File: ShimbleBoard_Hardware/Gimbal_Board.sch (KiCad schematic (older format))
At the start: 54 parts, among them Q1 2N3904, Q2 2N3904, Q3 2N3904, Q4 2N3904, Q5 2N3904, Q6 2N3904, Q7 2N3904, Q8 2N3904, U1 TM4C129E_Launchpad, U2 OKI, U3 OKI

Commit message: Noice
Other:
- note added: "Shimble Board"
- moved on the sheet: C1, C2, C3, C4, C5, C6, Conn9A, Conn9B, Conn9C

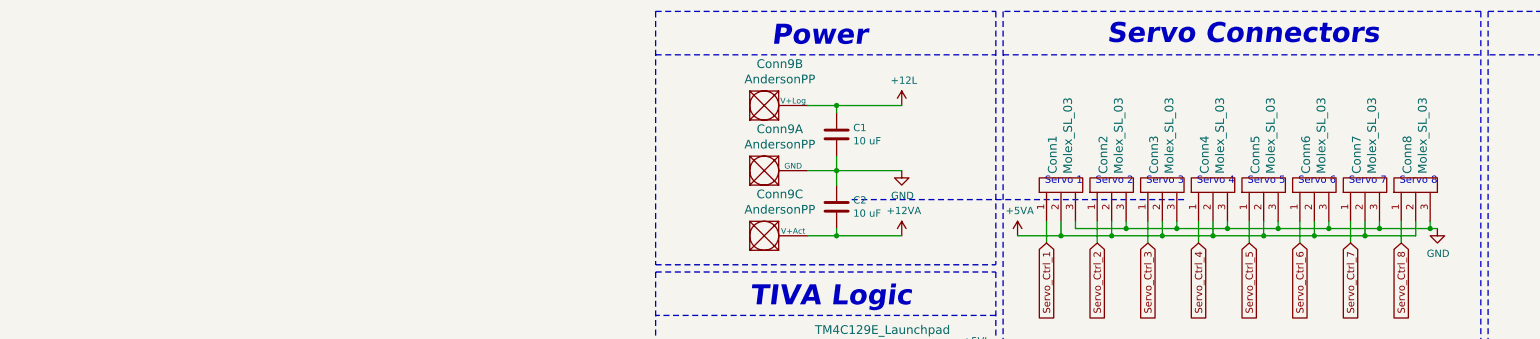
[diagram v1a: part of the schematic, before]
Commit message: Silkscreens Added
Signitures and logo was added.
Schematic cleaned up a little.
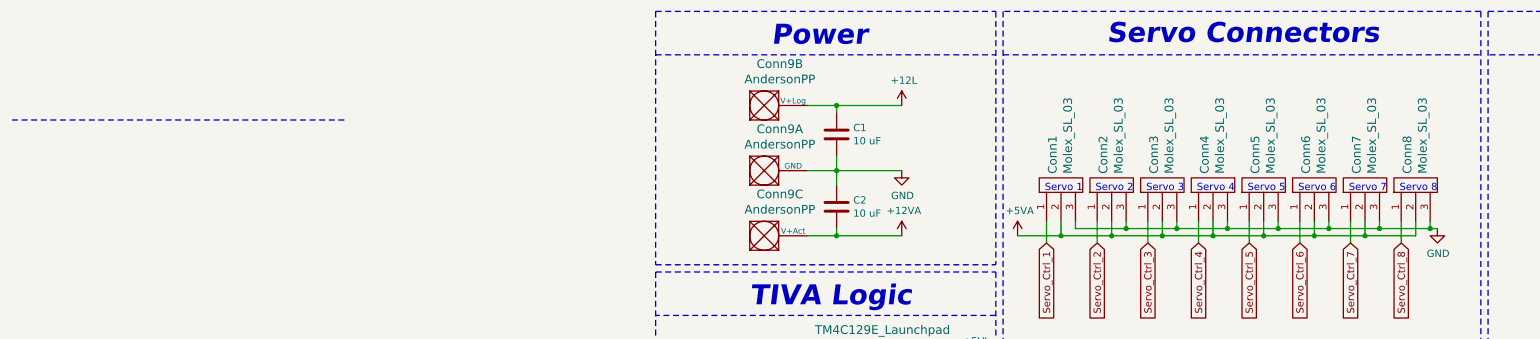
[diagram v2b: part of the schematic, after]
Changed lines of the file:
@@
 Wire Wire Line
 	4950 2950 4950 2800
-Text Notes 4150 2550 2    50   ~ 0
+Text Notes 4150 2600 2    50   ~ 0
 Servo 1
-Text Notes 4500 2550 2    50   ~ 0
+Text Notes 4500 2600 2    50   ~ 0
 Servo 2
-Text Notes 4850 2550 2    50   ~ 0
+Text Notes 4850 2600 2    50   ~ 0
 Servo 3
-Text Notes 5200 2550 2    50   ~ 0
+Text Notes 5200 2600 2    50   ~ 0
 Servo 4
-Text Notes 5550 2550 2    50   ~ 0
+Text Notes 5550 2600 2    50   ~ 0
 Servo 5
-Text Notes 5900 2550 2    50   ~ 0
+Text Notes 5900 2600 2    50   ~ 0
 Servo 6
 Connection ~ 5850 2850
@@
 	6600 2850 6550 2850
 Connection ~ 6550 2850
-Text Notes 6250 2550 2    50   ~ 0
+Text Notes 6250 2600 2    50   ~ 0
 Servo 7
-Text Notes 6600 2550 2    50   ~ 0
+Text Notes 6600 2600 2    50   ~ 0
 Servo 8
 Wire Notes Line
@@
 	6900 1350 3600 1350
 Wire Notes Line
-	4850 2650 2550 2650
+	-950 2100 -3250 2100
 Wire Notes Line
 	6900 1350 6900 3650

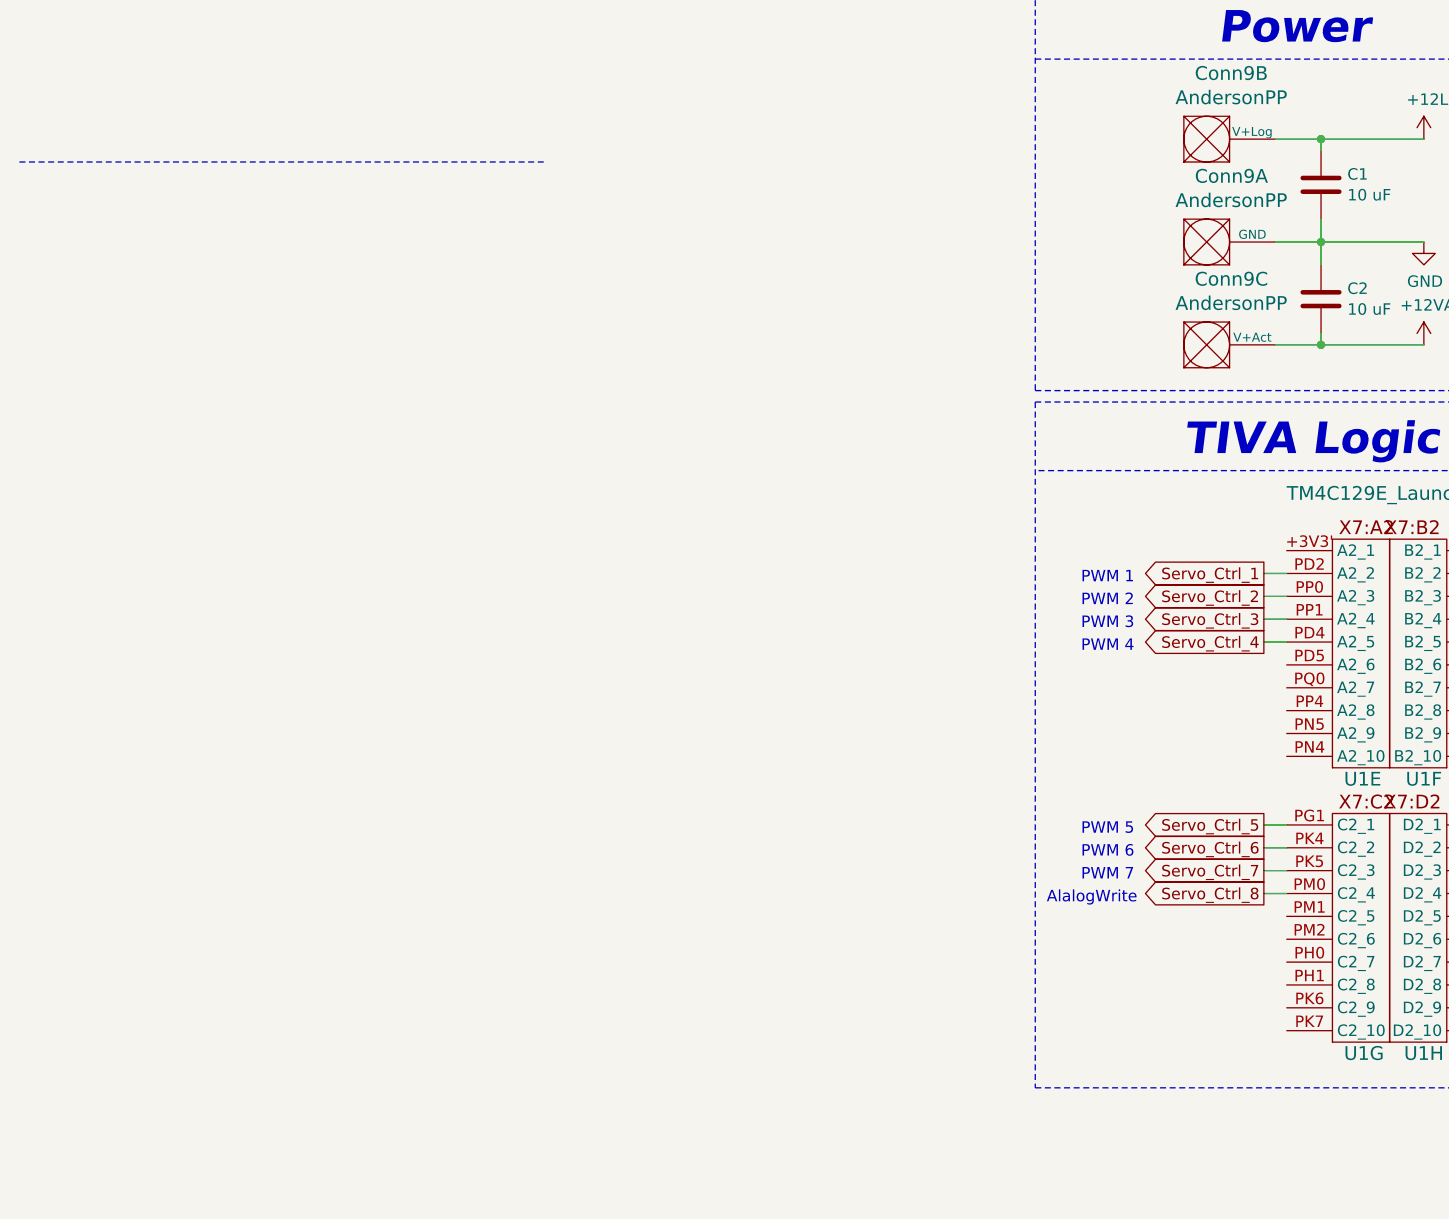
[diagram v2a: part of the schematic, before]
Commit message: Pins Fixed
PCB layout is also a bit cleaner
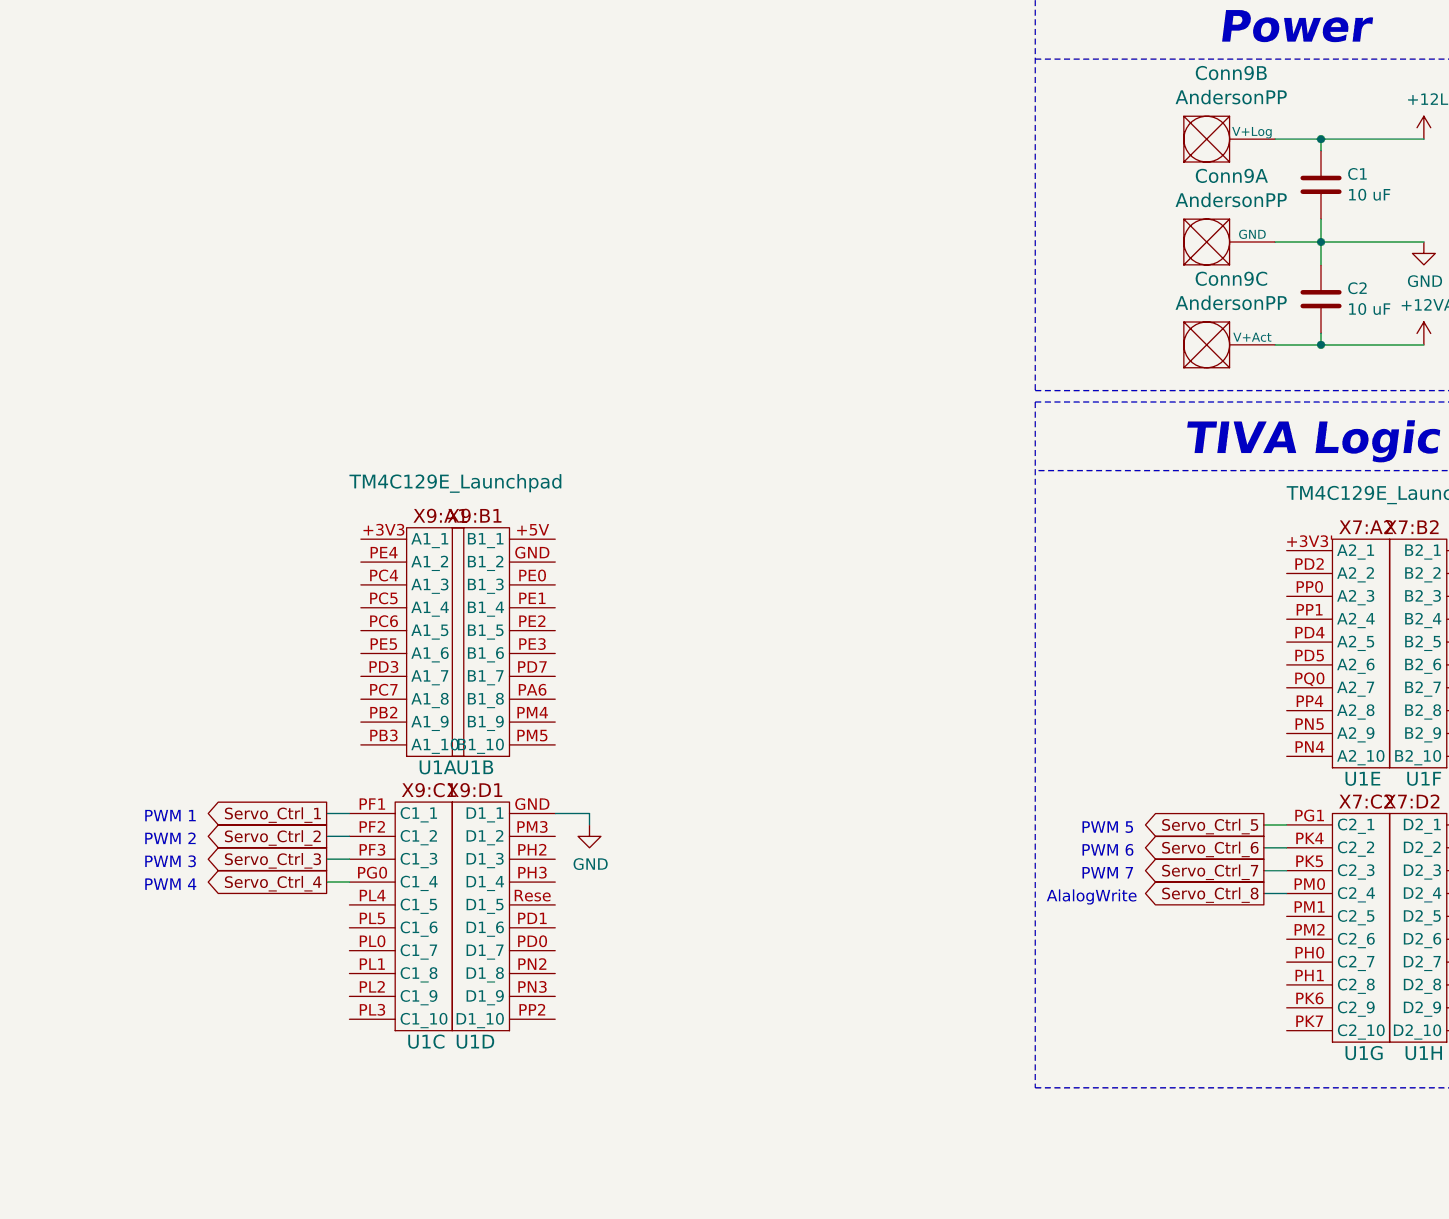
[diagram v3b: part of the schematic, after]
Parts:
- added unit 1 of U1
- added unit 2 of U1
- added unit 3 of U1
- added unit 4 of U1
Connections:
- net GND: now also U1.GND (D1_1)
- net Servo_Ctrl_1: now also U1.PF1 (C1_1); no longer U1.PD2 (A2_2)
- net Servo_Ctrl_2: now also U1.PF2 (C1_2); no longer U1.PP0 (A2_3)
- net Servo_Ctrl_3: now also U1.PF3 (C1_3); no longer U1.PP1 (A2_4)
- net Servo_Ctrl_4: now also U1.PG0 (C1_4); no longer U1.PD4 (A2_5)
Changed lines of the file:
@@
 Text Notes 1400 5050 0    50   ~ 0
 PWM 5
-Text Notes 1400 4250 0    50   ~ 0
+Text Notes -2700 5300 0    50   ~ 0
 PWM 4
-Text Notes 1400 4150 0    50   ~ 0
+Text Notes -2700 5200 0    50   ~ 0
 PWM 3
-Text Notes 1400 4050 0    50   ~ 0
+Text Notes -2700 5100 0    50   ~ 0
 PWM 2
-Text Notes 1400 3950 0    50   ~ 0
+Text Notes -2700 5000 0    50   ~ 0
 PWM 1
 Wire Wire Line
 	2200 5300 2300 5300
 Wire Wire Line
-	2300 3900 2200 3900
-Wire Wire Line
-	2200 4000 2300 4000
-Wire Wire Line
-	2300 4100 2200 4100
-Wire Wire Line
-	2200 4200 2300 4200
+	-1800 4950 -1900 4950
+Wire Wire Line
+	-1900 5050 -1800 5050
+Wire Wire Line
+	-1800 5150 -1900 5150
+Wire Wire Line
+	-1900 5250 -1800 5250
 Wire Notes Line
 	1200 3150 1200 6150
@@
 Text Notes 1850 3400 0    138  Italic 28
 TIVA Logic
-Text GLabel 2200 4200 0    50   Output ~ 0
+Text GLabel -1900 5250 0    50   Output ~ 0
 Servo_Ctrl_4
-Text GLabel 2200 4100 0    50   Output ~ 0
+Text GLabel -1900 5150 0    50   Output ~ 0
 Servo_Ctrl_3
-Text GLabel 2200 4000 0    50   Output ~ 0
+Text GLabel -1900 5050 0    50   Output ~ 0
 Servo_Ctrl_2
-Text GLabel 2200 3900 0    50   Output ~ 0
+Text GLabel -1900 4950 0    50   Output ~ 0
 Servo_Ctrl_1
 Wire Wire Line
@@
 	6900 1350 3600 1350
 Wire Notes Line
-	-950 2100 -3250 2100
-Wire Notes Line
 	6900 1350 6900 3650
 Wire Wire Line
@@
 Wire Notes Line
 	3600 1350 3600 3650
+$Comp
+L MRDT_Shields:TM4C129E_Launchpad U1
+U 1 1 5DA28D2E
+P -1550 4700
+F 0 "U1" H -1500 4650 60  0000 L CNN
+F 1 "TM4C129E_Launchpad" H -1800 5900 60  0000 L CNN
+F 2 "MRDT_Shields:TM4C129E_Launchpad_FULL_THT_BOTTOM" H -1550 4700 60  0001 C CNN
+F 3 "" H -1550 4700 60  0001 C CNN
+	1    -1550 4700
+	1    0    0    -1
+$EndComp
+$Comp
+L MRDT_Shields:TM4C129E_Launchpad U1
+U 2 1 5DA2BE1E
+P -1100 4700
+F 0 "U1" H -950 4650 60  0000 C CNN
+F 1 "TM4C129E_Launchpad" H -1069 5871 60  0001 C CNN
+F 2 "MRDT_Shields:TM4C129E_Launchpad_FULL_THT_BOTTOM" H -1100 4700 60  0001 C CNN
+F 3 "" H -1100 4700 60  0001 C CNN
+	2    -1100 4700
+	-1   0    0    -1
+$EndComp
+$Comp
+L MRDT_Shields:TM4C129E_Launchpad U1
+U 3 1 5DA2EA3D
+P -1600 5900
+F 0 "U1" H -1550 5850 60  0000 L CNN
+F 1 "TM4C129E_Launchpad" H -1295 6392 60  0001 L CNN
+F 2 "MRDT_Shields:TM4C129E_Launchpad_FULL_THT_BOTTOM" H -1600 5900 60  0001 C CNN
+F 3 "" H -1600 5900 60  0001 C CNN
+	3    -1600 5900
+	1    0    0    -1
+$EndComp
+$Comp
+L MRDT_Shields:TM4C129E_Launchpad U1
+U 4 1 5DA313FB
+P -1100 5900
+F 0 "U1" H -950 5850 60  0000 C CNN
+F 1 "TM4C129E_Launchpad" H -795 6392 60  0001 L CNN
+F 2 "MRDT_Shields:TM4C129E_Launchpad_FULL_THT_BOTTOM" H -1100 5900 60  0001 C CNN
+F 3 "" H -1100 5900 60  0001 C CNN
+	4    -1100 5900
+	-1   0    0    -1
+$EndComp
+Wire Wire Line
+	-750 4950 -900 4950
+Wire Wire Line
+	-750 5000 -750 4950
+$Comp
+L power:GND #PWR0107
+U 1 1 5DA8E928
+P -750 5000
+F 0 "#PWR0107" H -750 4750 50  0001 C CNN
+F 1 "GND" H -745 4827 50  0000 C CNN
+F 2 "" H -750 5000 50  0001 C CNN
+F 3 "" H -750 5000 50  0001 C CNN
+	1    -750 5000
+	1    0    0    -1
+$EndComp
 $EndSCHEMATC

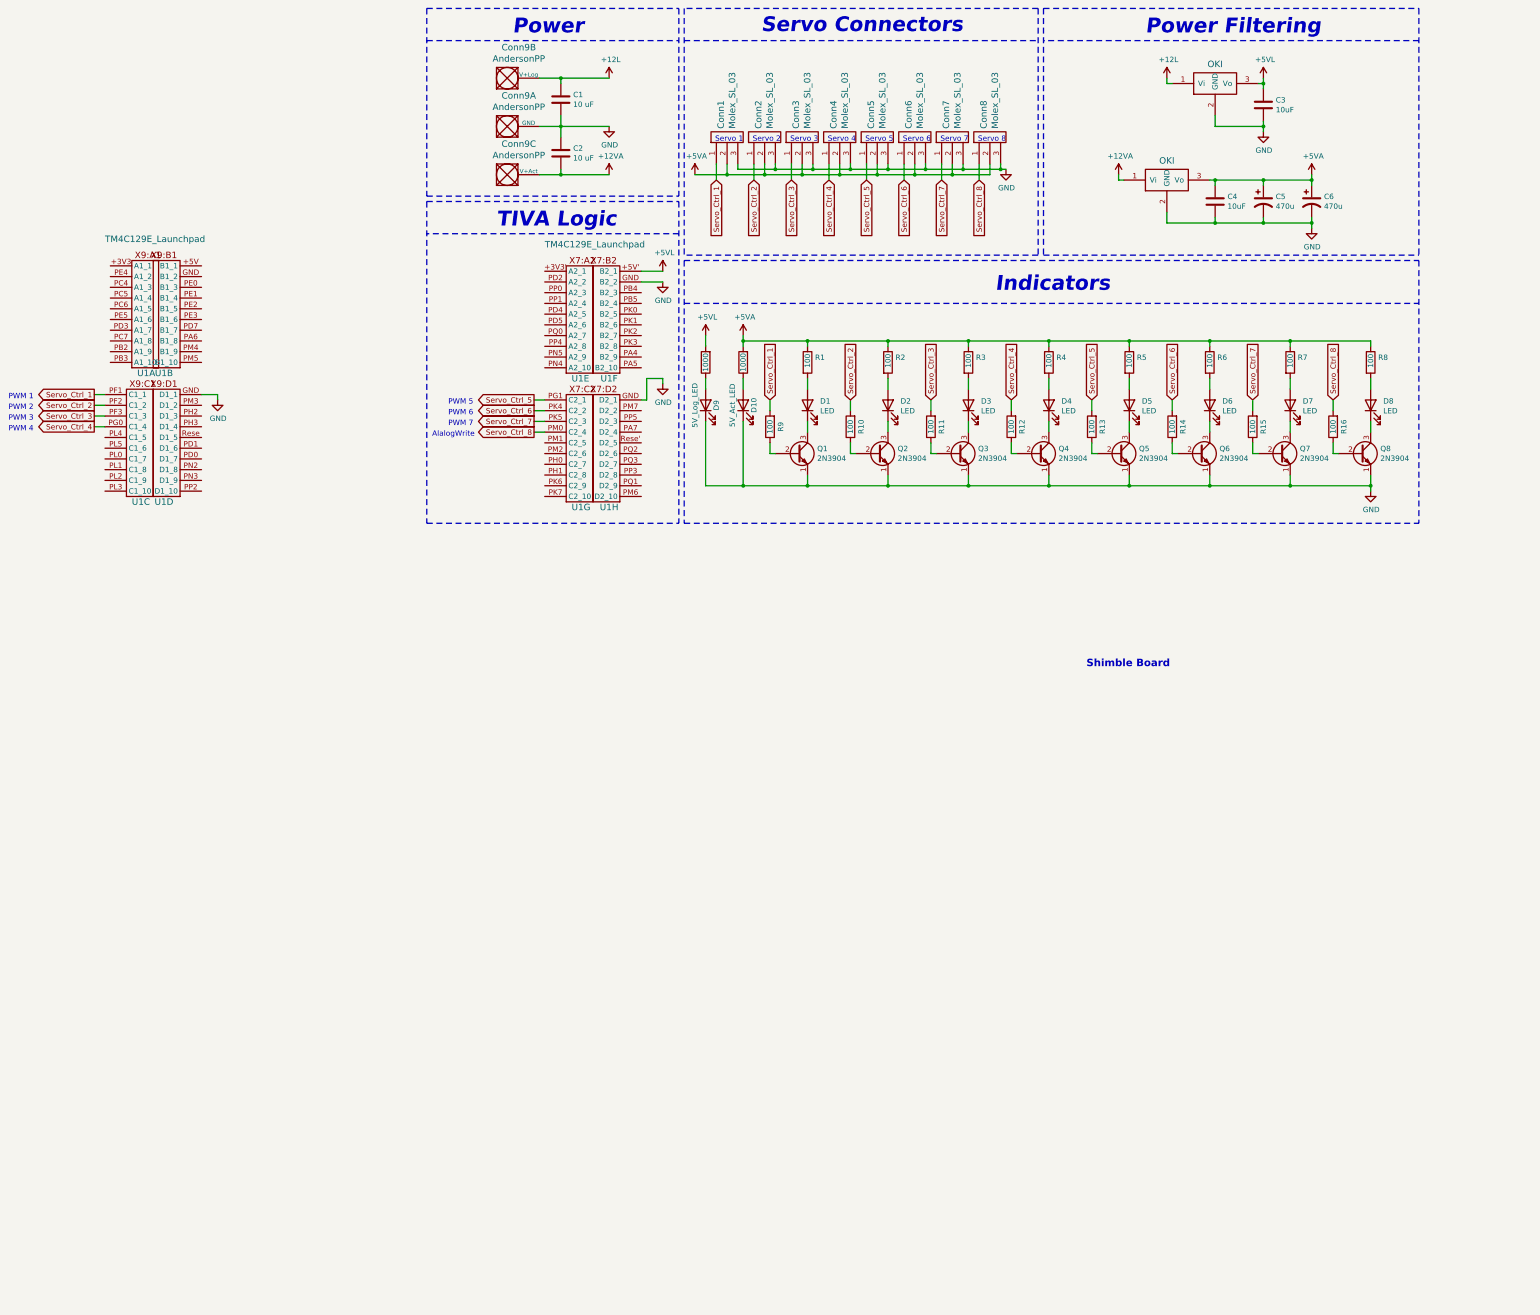
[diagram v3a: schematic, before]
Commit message: Cleaned up some wires
Back copper wires of the leftmost connecters.
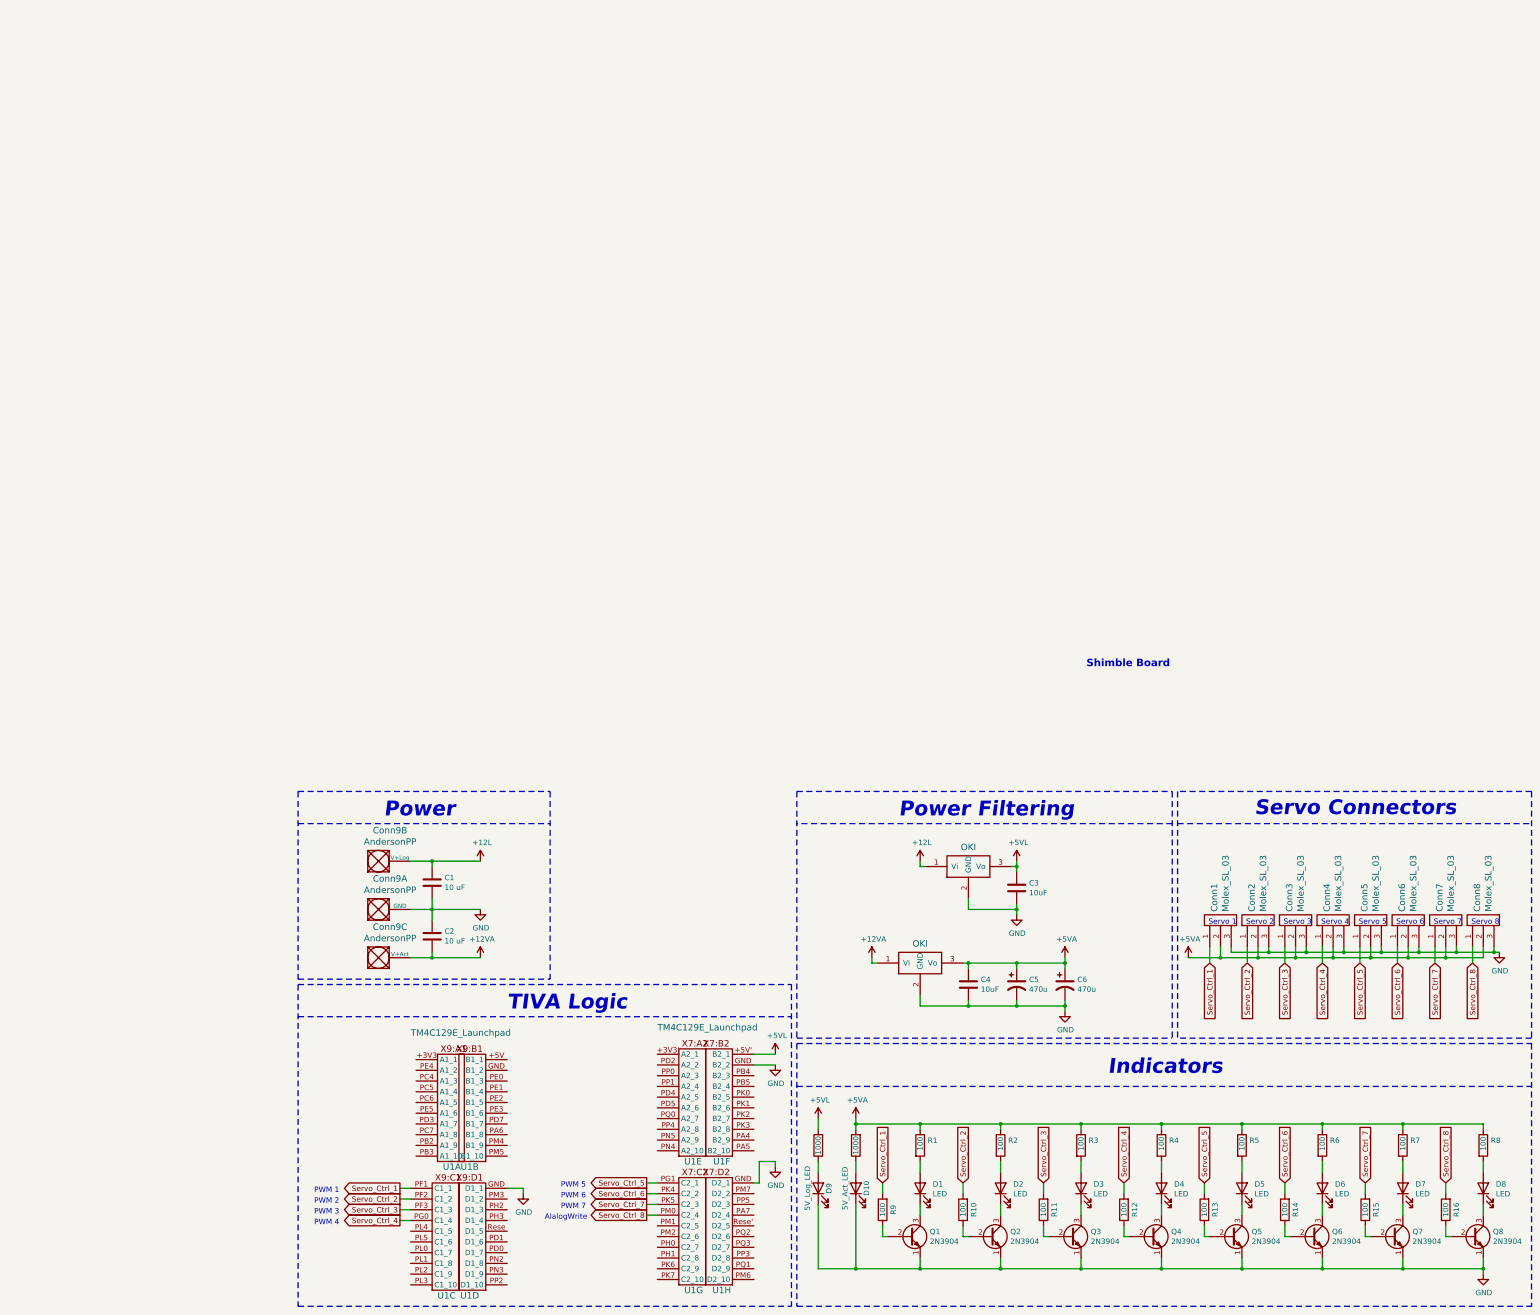
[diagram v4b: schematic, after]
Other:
- moved on the sheet: C1, C2, C3, C4, C5, C6, Conn1, Conn2, Conn3, Conn4, Conn5, Conn6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
